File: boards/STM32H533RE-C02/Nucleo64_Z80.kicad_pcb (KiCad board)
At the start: 2 copper layers, 68.6 x 53.3 mm, 29 parts, among them J1 Conn_01x20_Pin, J2 Conn_01x20_Pin, J3 Qwiic_connector, J4 SD Card slot, J5 SD Card slot, U2 AS6C4008-55PCN, U3 Z80CPU, U4 74LS125

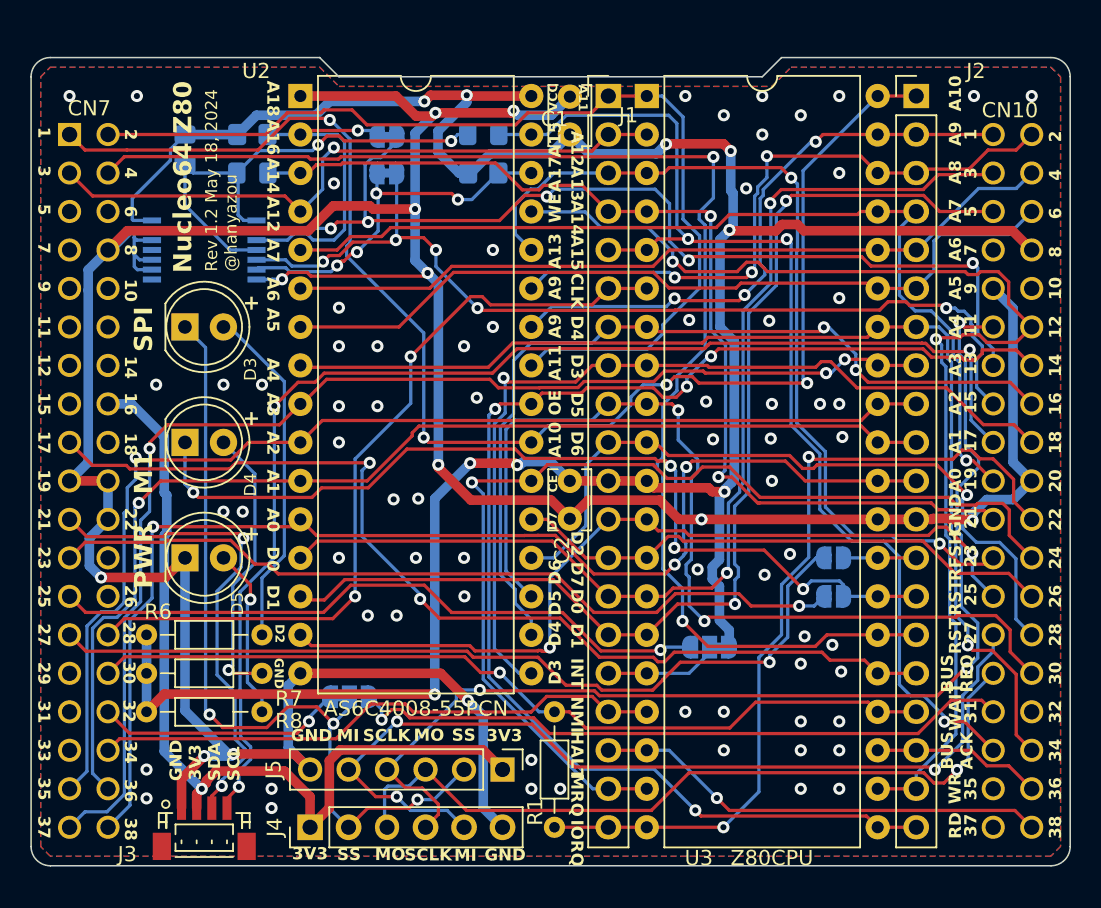
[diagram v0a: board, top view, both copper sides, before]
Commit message: stm32h533re: Fix PCB layout
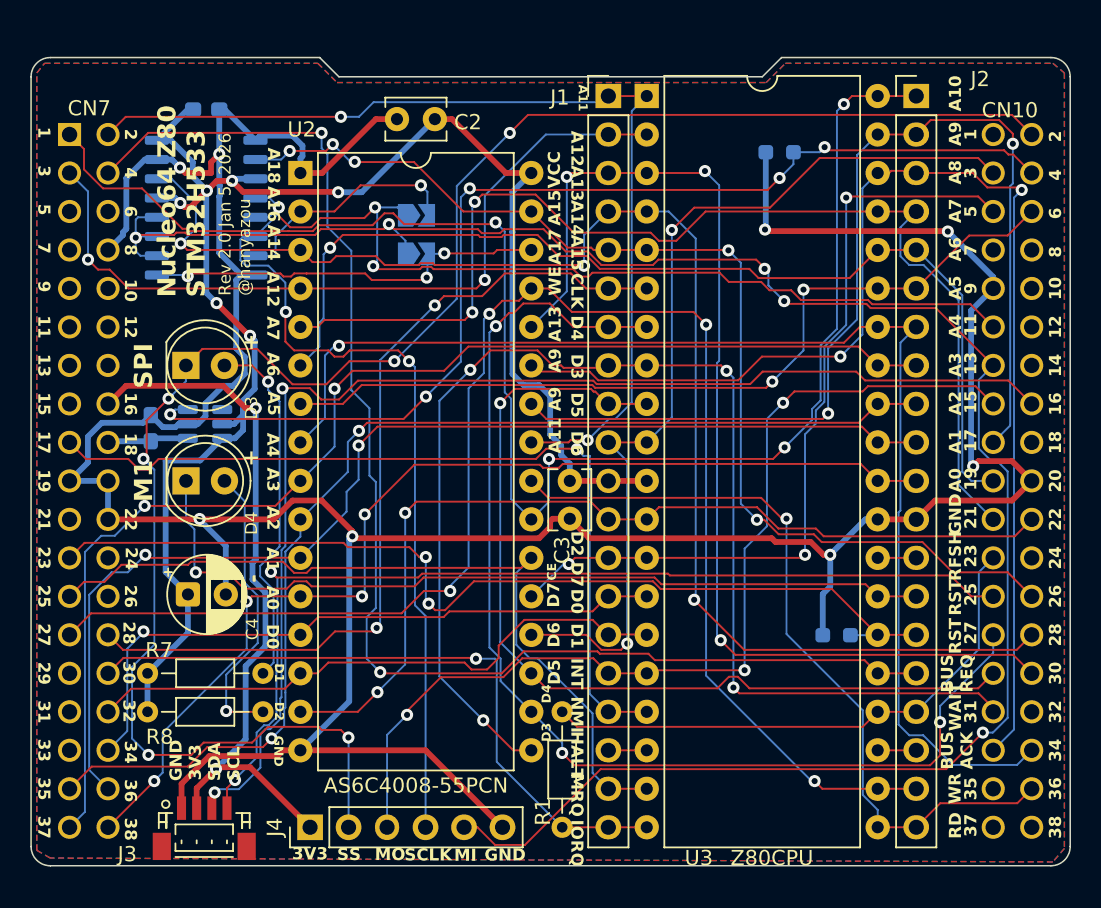
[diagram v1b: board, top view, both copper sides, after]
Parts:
- removed D1, D2: 1N4001, Diode_SMD:D_0805_2012Metric_Pad1.15x1.40mm_HandSolder
- removed D5: LED, LED_THT:LED_D5.0mm
- removed J5: SD Card slot, Connector_PinHeader_2.54mm:PinHeader_1x06_P2.54mm_Vertical
- removed the JP1 at (126.4, 136.2)
- removed the JP2 at (150.2, 132.9)
- removed JP3, JP4: SolderJumper_2_Open, Jumper:SolderJumper-2_P1.3mm_Open_RoundedPad1.0x1.5mm
- removed R4: 10K, Resistor_SMD:R_0805_2012Metric_Pad1.20x1.40mm_HandSolder
- removed the R8 at (113.0, 137.2)
- added C1: 0.1uF, Capacitor_SMD:C_0603_1608Metric_Pad1.08x0.95mm_HandSolder, B.Cu at (113.3, 118.4)
- added C4: 10uF, Capacitor_THT:CP_Radial_D5.0mm_P2.50mm, F.Cu at (115.8, 129.4)
- added C5: 0.1uF, Capacitor_SMD:C_0603_1608Metric_Pad1.08x0.95mm_HandSolder, B.Cu at (117.0, 97.4)
- added U5: 74LS153, Package_SO:SOP-16_4.55x10.3mm_P1.27mm, B.Cu at (117.0, 103.9)
- JP1: renamed from JP5; value SolderJumper_2_Bridged -> SolderJumper_2; footprint Jumper:SolderJumper-2_P1.3mm_Bridged_RoundedPad1.0x1.5mm -> Jumper:SolderJumper-2_P1.3mm_Open_TrianglePad1.0x1.5mm
- JP2: renamed from JP6; value SolderJumper_2_Bridged -> SolderJumper_2; footprint Jumper:SolderJumper-2_P1.3mm_Bridged_RoundedPad1.0x1.5mm -> Jumper:SolderJumper-2_P1.3mm_Open_TrianglePad1.0x1.5mm
- R2: value 1K -> 10K; footprint Resistor_SMD:R_0805_2012Metric_Pad1.20x1.40mm_HandSolder -> Resistor_SMD:R_0603_1608Metric_Pad0.98x0.95mm_HandSolder
- R3: footprint Resistor_SMD:R_0805_2012Metric_Pad1.20x1.40mm_HandSolder -> Resistor_SMD:R_0603_1608Metric_Pad0.98x0.95mm_HandSolder
- U4: value 74LS125 -> TPS22917DBV; footprint Package_SO:SSOP-14_5.3x6.2mm_P0.65mm -> Package_TO_SOT_SMD:SOT-23-6
- moved R2 53.6 mm to (158.6, 132.1), turned to 180 degrees
- moved R3 34.8 mm to (154.8, 100.2), turned to 180 degrees
- moved U4 11.5 mm to (116.9, 118.2), turned to 0 degrees
- moved C2 8.97 mm to (132.1, 98.0), turned to 180 degrees
- moved JP2 5.68 mm to (130.8, 106.9), turned to 0 degrees
- moved JP1 5.56 mm to (130.8, 104.4), turned to 0 degrees
- moved U2 5.08 mm to (123.2, 101.6)
- moved D4 2.54 mm to (115.6, 121.9)
- moved D3 2.54 mm to (115.6, 114.3)
- moved R7 2.54 mm to (113.1, 134.6)
- moved R8 2.54 mm to (113.1, 137.2)
- moved R1 0.51 mm to (140.5, 137.2)
- renumbered C1 to C2, C2 to C3, R6 to R7, R7 to R8
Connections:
- J1 pad 16: ~{INT} -> SPI1_MOSI
- J4 pad 4: SPI1_SCLK -> BANK_SEL0
- J4 pad 5: SPI1_MISO -> BANK_SEL1
- R2 pad 1: VCC -> ~{RESET}
- R2 pad 2: Net-(D1-A) -> GND
- R3 pad 1: VCC -> Z80_PWR_EN
- R3 pad 2: A16 -> GND
- U1 pad CN10_1: A9 -> unconnected-(U1-NC-PadCN10_1)
- U1 pad CN10_11: SPI1_SCLK -> BANK_SEL0
- U1 pad CN10_12: ~{WR} -> unconnected-(U1-PA_12-PadCN10_12)
- U1 pad CN10_13: BANK_SEL0 -> BANK_SEL1
- U1 pad CN10_14: ~{RD} -> unconnected-(U1-PA_11-PadCN10_14)
- U1 pad CN10_15: BANK_SEL1 -> SPI1_MOSI
- U1 pad CN10_16: D4 -> I2C1_SDA
- U1 pad CN10_17: I2C1_SCL -> A9
- U1 pad CN10_18: D3 -> unconnected-(U1-NC-PadCN10_18)
- U1 pad CN10_19: A7 -> A6
- U1 pad CN10_2: A8 -> ~{SPI1_SS}
- U1 pad CN10_21: A14 -> A7
- U1 pad CN10_22: ~{IORQ} -> D2
- U1 pad CN10_23: A13 -> ~{WAIT}
- U1 pad CN10_24: ~{MREQ} -> unconnected-(U1-NC-PadCN10_24)
- U1 pad CN10_25: D2 -> I2C1_SCL
- U1 pad CN10_26: D7 -> A15
- U1 pad CN10_27: SPI1_MISO -> D4
- U1 pad CN10_28: D6 -> A14
- U1 pad CN10_29: SPI1_MOSI -> D5
- U1 pad CN10_3: D0 -> D6
- U1 pad CN10_30: D5 -> A13
- U1 pad CN10_31: PB3 -> D3
- U1 pad CN10_33: A15 -> A8
- U1 pad CN10_36: ~{BUSACK} -> ~{RD}
- U1 pad CN10_38: ~{HALT} -> unconnected-(U1-NC-PadCN10_38)
- U1 pad CN10_4: A6 -> Z80_PWR_EN
- U1 pad CN10_5: D1 -> D7
- U1 pad CN10_8: VCC -> unconnected-(U1-VBUS_STLK-PadCN10_8)
- U1 pad CN7_17: ~{BUSRQ} -> ~{NMI}
- U1 pad CN7_18: unconnected-(U1-5V-PadCN7_18) -> 5V
- U1 pad CN7_21: I2C1_SDA -> unconnected-(U1-NC-PadCN7_21)
- U1 pad CN7_23: PC13 -> ~{RESET}
- U1 pad CN7_25: PC14 -> ~{MREQ}
- U1 pad CN7_27: PC15 -> ~{WR}
- U1 pad CN7_30: ~{WAIT} -> ~{IORQ}
- U1 pad CN7_32: PA4 -> D1
- U1 pad CN7_34: ~{NMI} -> D0
- U1 pad CN7_4: ~{RESET} -> ~{BUSRQ}
- U3 pad 16: ~{INT} -> SPI1_MOSI
- U4 pad 1: Net-(D1-A) -> 5V
- U4 pad 2: BANK_SEL0 -> GND
- U4 pad 3: A16 -> Z80_PWR_EN
- U4 pad 4: Net-(D1-A) -> unconnected-(U4-CT-Pad4)
- U4 pad 5: BANK_SEL1 -> VCC
- U4 pad 6: A17 -> VCC
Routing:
- net SPI1_SCLK: track 74.9 -> 0.00 mm, vias 3 -> 0
- net Z80_PWR_EN: track 0.00 -> 73.3 mm, vias 0 -> 5
- net BANK_SEL1: track 62.5 -> 135.4 mm
- net ~{SPI1_SS}: track 55.2 -> 117.9 mm, vias 3 -> 6
- net VCC: track 172.8 -> 111.0 mm, vias 9 -> 6
- net SPI1_MISO: track 61.6 -> 0.00 mm, vias 3 -> 0
- net PC15: track 57.2 -> 0.00 mm, vias 1 -> 0
- net PC13: track 53.3 -> 0.00 mm, vias 1 -> 0
- net I2C1_SDA: track 32.4 -> 82.4 mm
- net BANK_SEL0: track 66.6 -> 113.3 mm
- net PB3: track 44.4 -> 0.00 mm, vias 1 -> 0
- net PC14: track 44.0 -> 0.00 mm, vias 1 -> 0
- net A8: track 42.7 -> 82.6 mm, vias 3 -> 2
- net ~{RD}: track 89.2 -> 52.0 mm, vias 4 -> 1
- net D1: track 74.2 -> 39.4 mm, vias 2 -> 0
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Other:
- board text added: "-"
- board text added: "Nucleo64 Z80 STM32H533"
- board text added: "Rev 2.0 Jan 5, 2026 @hanyazou"
- board text removed: "Nucleo64 Z80"
- board text removed: "OE"
- board text removed: "PWR"
- board text removed: "Rev 1.2 May 18, 2024 @hanyazou"
